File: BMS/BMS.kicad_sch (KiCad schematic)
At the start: 2 parts, among them IC1 L9963E-TR

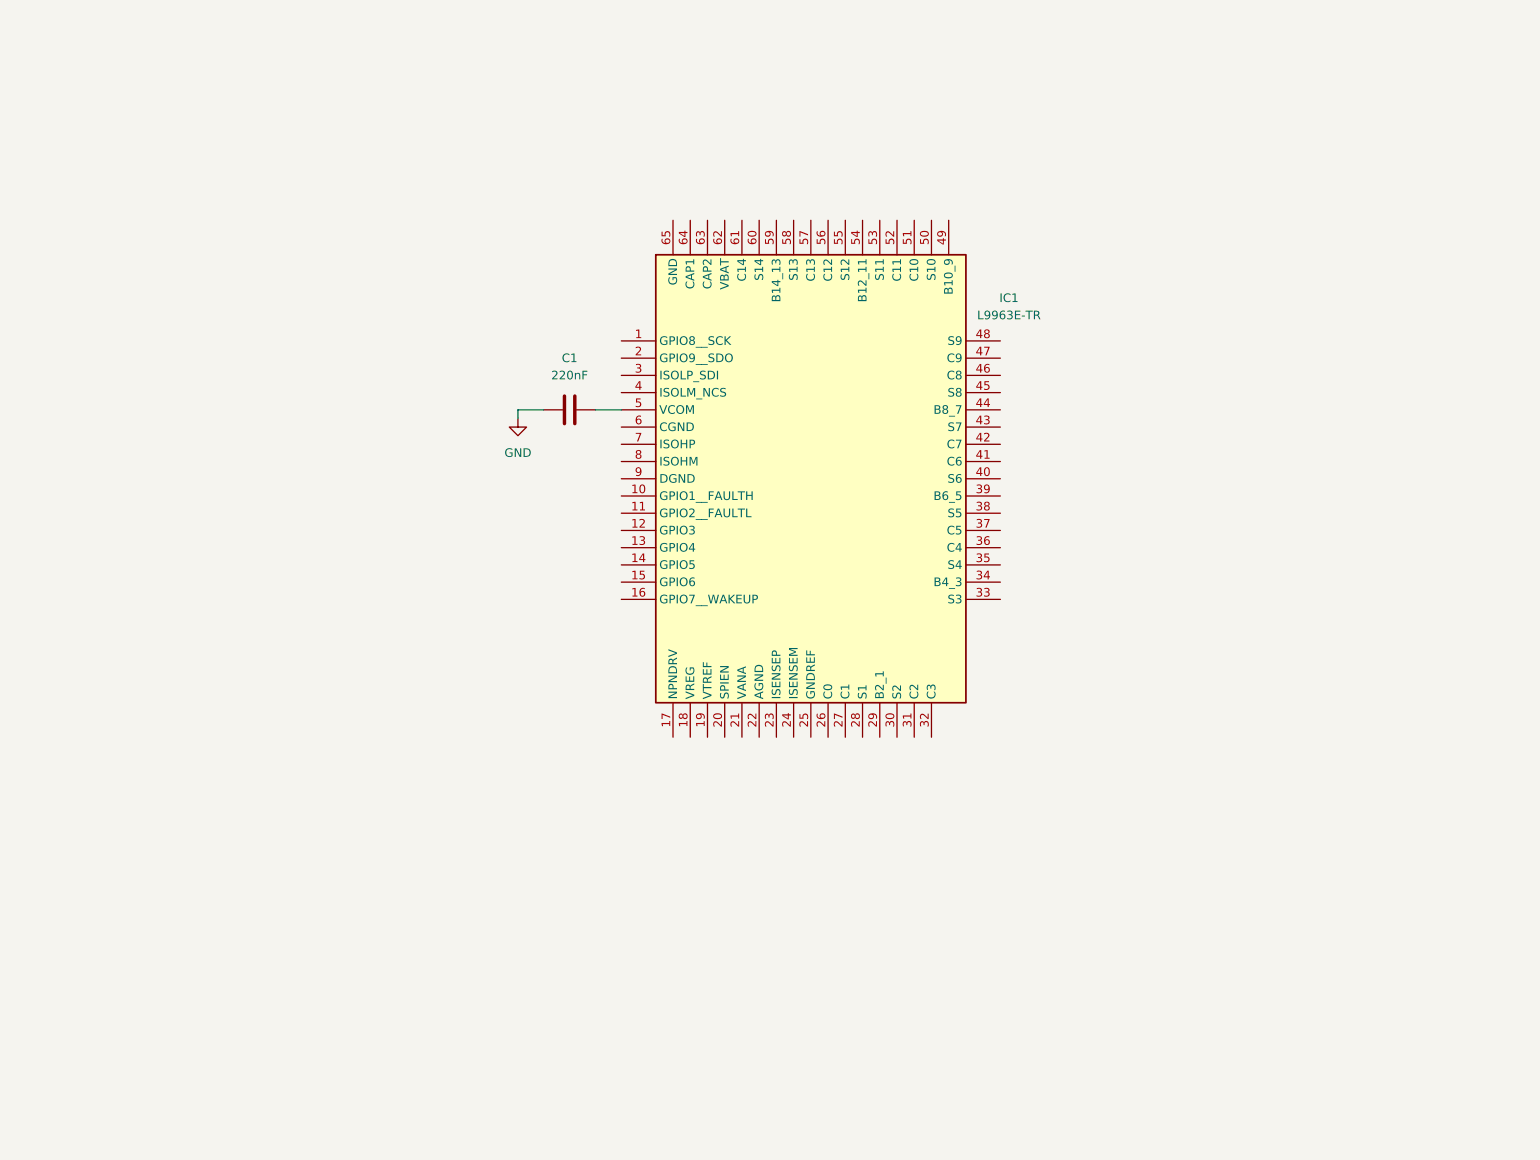
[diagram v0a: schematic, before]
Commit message: updated schematic (partially completed)
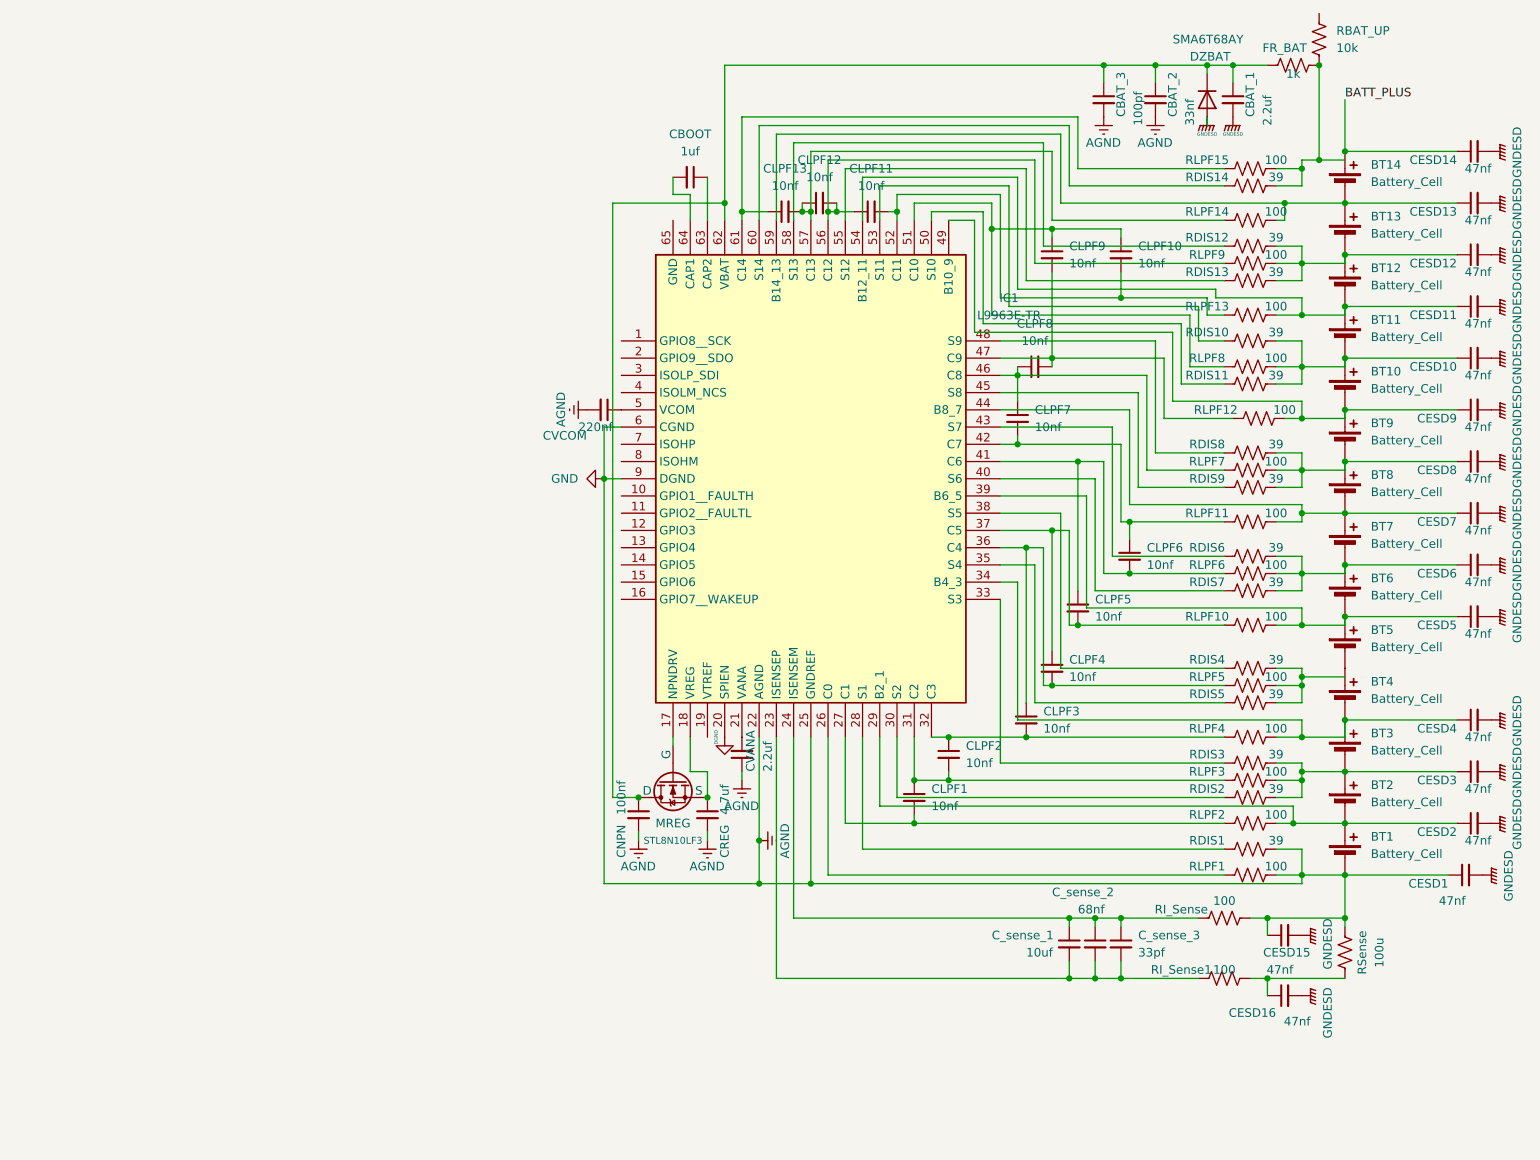
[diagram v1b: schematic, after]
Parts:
- removed C1: 220nF, symbol Device:C
- added 10uf: C_sense_1, symbol Device:C_Small
- added 33pf: C_sense_3, symbol Device:C_Small
- added 4.7uf: CREG, symbol Device:C_Small
- added 68nf: C_sense_2, symbol Device:C_Small
- added BT1, BT10, BT11, BT12, BT13, BT14, BT2, BT3, BT4, BT5, BT6, BT7, BT8, BT9: Battery_Cell, symbol Device:Battery_Cell
- added CBAT_1, CVANA: 2.2uf, symbol Device:C_Small
- added CBAT_2: 33nf, symbol Device:C_Small
- added CBAT_3: 100pf, symbol Device:C_Small
- added CBOOT: 1uf, symbol Device:C_Small
- added CESD1, CESD10, CESD11, CESD12, CESD13, CESD14, CESD15, CESD16, CESD2, CESD3, CESD4, CESD5, CESD6, CESD7, CESD8, CESD9: 47nf, symbol Device:C_Small
- added CLPF1, CLPF10, CLPF11, CLPF12, CLPF13, CLPF2, CLPF3, CLPF4, CLPF5, CLPF6, CLPF7, CLPF8, CLPF9: 10nf, symbol Device:C_Small
- added CNPN: 100nf, symbol Device:C_Small
- added CVCOM: 220nf, symbol Device:C_Small
- added DZBAT: SMA6T68AY, symbol Device:D
- added FR_BAT: 1k, symbol Device:R_US
- added MREG: STL8N10LF3, symbol Simulation_SPICE:NMOS
- added RBAT_UP: 10k, symbol Device:R_US
- added RDIS1, RDIS10, RDIS11, RDIS12, RDIS13, RDIS14, RDIS2, RDIS3, RDIS4, RDIS5, RDIS6, RDIS7, RDIS8, RDIS9: 39, symbol Device:R_US
- added RI_Sense, RI_Sense1, RLPF1, RLPF10, RLPF11, RLPF12, RLPF13, RLPF14, RLPF15, RLPF2, RLPF3, RLPF4, RLPF5, RLPF6, RLPF7, RLPF8, RLPF9: 100, symbol Device:R_US
- added RSense: 100u, symbol Device:R_US
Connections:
- net at IC1.17 (NPNDRV): now also MREG.2 (G)
- net at IC1.18 (VREG): now also 4.7uf.1, MREG.3 (S)
- net DGND: now reaches IC1.20 (SPIEN)
- net at IC1.21 (VANA): now also CVANA.2
- net AGND: now reaches IC1.22 (AGND)
- net AGND: now also IC1.25 (GNDREF), IC1.6 (CGND), IC1.9 (DGND), 4.7uf.2, BT1.2 (-), CBAT_2.2, CBAT_3.2, CESD1.1, CESD15.1, CNPN.2, CVANA.1, CVCOM.2, RDIS1.2, RI_Sense.2, RLPF1.2, RSense.1
- net at IC1.23 (ISENSEP): now also 10uf.2, 33pf.2, 68nf.2, RI_Sense1.1
- net at IC1.24 (ISENSEM): now also 10uf.1, 33pf.1, 68nf.1, RI_Sense.1
- net at IC1.26 (C0): now also RLPF1.1
- net at IC1.27 (C1): now also CLPF1.2, RLPF2.1
- net at IC1.28 (S1): now also RDIS1.1
- net at IC1.29 (B2_1): now also BT1.1 (+), BT2.2 (-), CESD2.1, RLPF2.2
- net at IC1.30 (S2): now also RDIS2.1
- net at IC1.31 (C2): now also CLPF1.1, CLPF2.2, RLPF3.1
- net at IC1.32 (C3): now also CLPF2.1, CLPF3.2, RLPF4.1
- net at IC1.33 (S3): now also RDIS3.1
- net at IC1.34 (B4_3): now also BT3.1 (+), BT4.2 (-), CESD4.1, RLPF4.2
- net at IC1.35 (S4): now also RDIS5.1
- net at IC1.36 (C4): now also CLPF3.1, CLPF4.2, RLPF5.1
- net at IC1.37 (C5): now also CLPF4.1, CLPF5.2, RLPF10.1
- net at IC1.38 (S5): now also RDIS4.1
- net at IC1.39 (B6_5): now also BT5.1 (+), BT6.2 (-), CESD5.1, RLPF10.2
- net at IC1.40 (S6): now also RDIS7.1
- net at IC1.41 (C6): now also CLPF5.1, CLPF6.2, RLPF6.1
- net at IC1.42 (C7): now also CLPF6.1, CLPF7.2, RLPF11.1
- net at IC1.43 (S7): now also RDIS6.1
- net at IC1.44 (B8_7): now also BT7.1 (+), BT8.2 (-), CESD7.1, RLPF11.2
- net at IC1.45 (S8): now also RDIS9.1
- net at IC1.46 (C8): now also CLPF7.1, CLPF8.1, RLPF7.1
- net at IC1.47 (C9): now also CLPF8.2, CLPF9.2, RLPF12.1
- net at IC1.48 (S9): now also RDIS8.1
- net at IC1.49 (B10_9): now also BT10.2 (-), BT9.1 (+), CESD9.1, RLPF12.2
- net at IC1.5 (VCOM): now also CVCOM.1
- net at IC1.50 (S10): now also RDIS11.1
- net at IC1.51 (C10): now also CLPF10.1, CLPF9.1, RLPF8.1
- net at IC1.52 (C11): now also CLPF10.2, CLPF11.2, RLPF13.1
- net at IC1.53 (S11): now also RDIS10.1
- net at IC1.54 (B12_11): now also BT11.1 (+), BT12.2 (-), CESD11.1, RLPF13.2
- net at IC1.55 (S12): now also RDIS13.1
- net at IC1.56 (C12): now also CLPF11.1, CLPF12.2, RLPF9.1
- net at IC1.57 (C13): now also CLPF12.1, CLPF13.2, RLPF14.1
- net at IC1.58 (S13): now also RDIS12.1
- net at IC1.59 (B14_13): now also BT13.1 (+), BT14.2 (-), CESD13.1, RLPF14.2
- net at IC1.60 (S14): now also RDIS14.1
- net at IC1.61 (C14): now also CLPF13.1, RLPF15.1
- net at IC1.62 (VBAT): now also CBAT_1.1, CBAT_2.1, CBAT_3.1, CNPN.1, DZBAT.1 (K), FR_BAT.1, MREG.1 (D)
- net at IC1.63 (CAP2): now also CBOOT.1
- net at IC1.64 (CAP1): now also CBOOT.2
- new net: BT6.1 (+), BT7.2 (-), CESD6.1, RDIS6.2, RDIS7.2, RLPF6.2
- new net: CESD16.1, RI_Sense1.2, RSense.2
- new net: BT2.1 (+), BT3.2 (-), CESD3.1, RDIS2.2, RDIS3.2, RLPF3.2
- new net: BT10.1 (+), BT11.2 (-), CESD10.1, RDIS10.2, RDIS11.2, RLPF8.2
- new net: BT8.1 (+), BT9.2 (-), CESD8.1, RDIS8.2, RDIS9.2, RLPF7.2
- new net: BT12.1 (+), BT13.2 (-), CESD12.1, RDIS12.2, RDIS13.2, RLPF9.2
- new net: RDIS4.2, RDIS5.2, RLPF5.2
- new net: FR_BAT.2, RBAT_UP.1, RDIS14.2, RLPF15.2
- new net: BT4.1 (+), BT5.2 (-)
- new net BATT_PLUS: BT14.1 (+), CESD14.1
- new net GNDESD: CBAT_1.2, CESD1.2, CESD10.2, CESD11.2, CESD12.2, CESD13.2, CESD14.2, CESD15.2, CESD16.2, CESD2.2, CESD3.2, CESD4.2, CESD5.2, CESD6.2, CESD7.2, CESD8.2, CESD9.2, DZBAT.2 (A)

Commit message: QoL + minor edits for future
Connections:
- net AGND: now also IC1.65 (GND)
- net at 4.7uf.1, IC1.18 (VREG), MREG.3 (S): now also IC1.17 (NPNDRV), IC1.19 (VTREF), MREG.2 (G)
- net BATT_PLUS: no longer names the net of BT14.1 (+), CESD14.1
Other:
- note added: "Battery+"
- note added: "GPIO connection"
- note added: "Unknown GND type"
- moved on the sheet: 10uf, 33pf, 4.7uf, 68nf, BT1, BT10, BT11, BT12, BT13, BT14, BT2, BT3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
